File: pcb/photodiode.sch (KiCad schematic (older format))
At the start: 9 parts, among them U6 photodiode, U7 LM324N

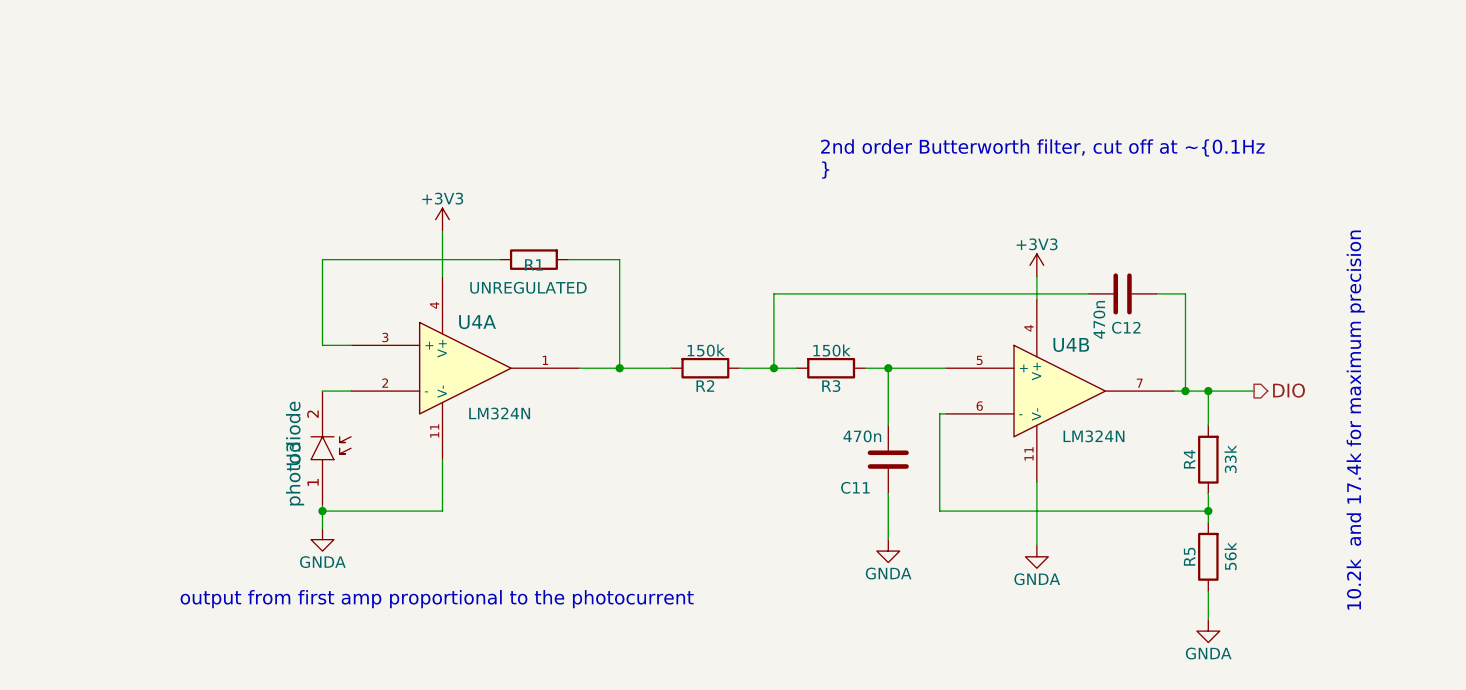
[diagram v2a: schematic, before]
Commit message: Changes to board, add footprints
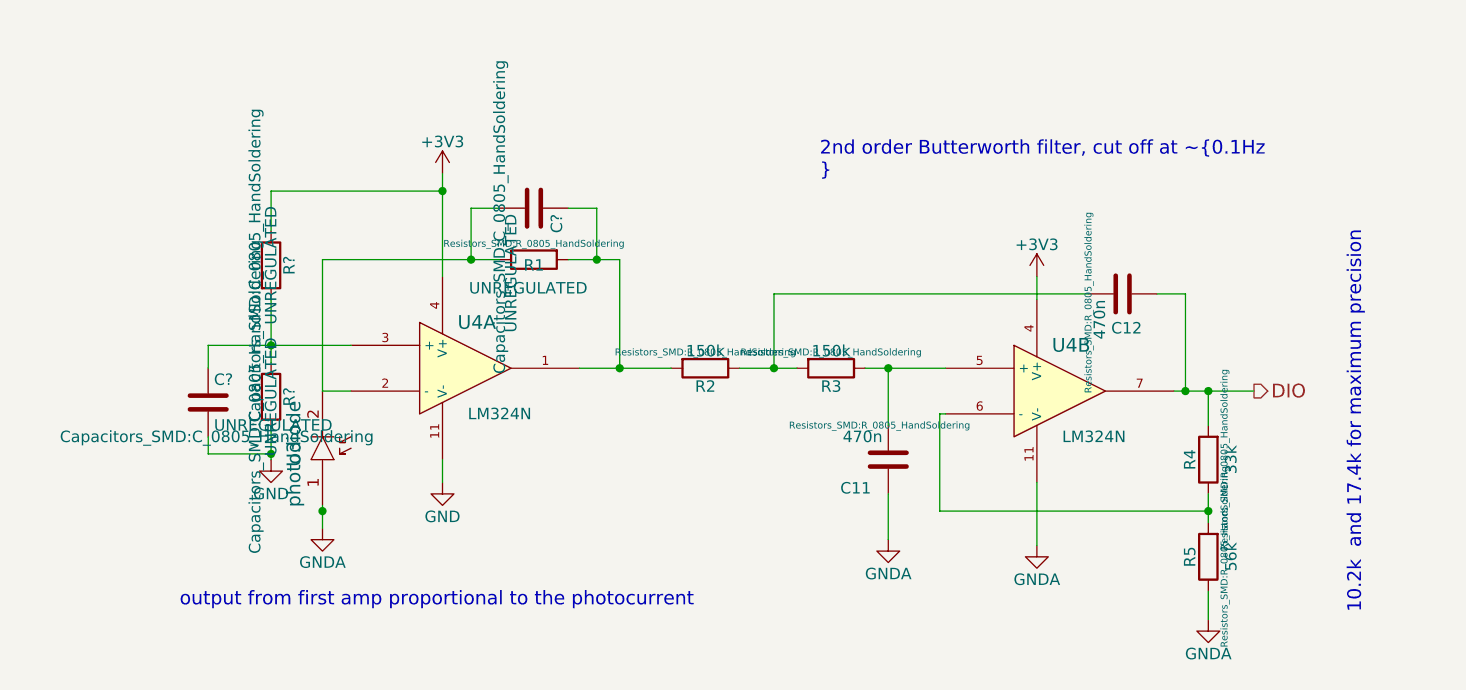
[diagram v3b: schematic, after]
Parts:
- added C? (x2): UNREGULATED, Capacitors_SMD:C_0805_HandSoldering, symbol C
- added R? (x2): UNREGULATED, Capacitors_SMD:C_0805_HandSoldering, symbol R
- C11, C16, R11, R12, R13, R14, R15: footprint (none) -> Resistors_SMD:R_0805_HandSoldering
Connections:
- net +3V3: now also R?.1
- net GNDA: no longer U7.11 (V-)
- net at U6.2 (C), U7.2 (-): now also R11.1, C?.2
- net at U7.3 (+): now also C?.1, R?.1, R?.2; no longer R11.1
- net at R11.2, R12.2, U7.1: now also C?.1
- new net GND: C?.2, R?.2, U7.11 (V-)
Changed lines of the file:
@@
 F 0 "R1" V 4425 2750 50  0000 C CNN
 F 1 "UNREGULATED" V 4525 2775 50  0000 C CNN
-F 2 "" V 4330 2750 30  0000 C CNN
+F 2 "Resistors_SMD:R_0805_HandSoldering" V 4330 2750 30  0000 C CNN
 F 3 "" H 4400 2750 30  0000 C CNN
 	1    4400 2750
@@
 L +3V3 #PWR40
 U 1 1 55BD9EDC
-P 4000 2625
+P 4000 2375
 AR Path="/55BDA44F/55BD9EDC" Ref="#PWR40"  Part="1"
 AR Path="/55BD9D56/55BD9EDC" Ref="#PWR28"  Part="1"
 AR Path="/55BDA313/55BD9EDC" Ref="#PWR34"  Part="1"
 AR Path="/55BDA511/55BD9EDC" Ref="#PWR46"  Part="1"
-F 0 "#PWR28" H 4000 2475 50  0001 C CNN
-F 1 "+3V3" H 4000 2765 50  0000 C CNN
-F 2 "" H 4000 2625 60  0000 C CNN
-F 3 "" H 4000 2625 60  0000 C CNN
-	1    4000 2625
+F 0 "#PWR28" H 4000 2225 50  0001 C CNN
+F 1 "+3V3" H 4000 2515 50  0000 C CNN
+F 2 "" H 4000 2375 60  0000 C CNN
+F 3 "" H 4000 2375 60  0000 C CNN
+	1    4000 2375
 	1    0    0    -1
 $EndComp
@@
 F 0 "R3" V 5780 3225 50  0000 C CNN
 F 1 "150k" V 5625 3225 50  0000 C CNN
-F 2 "" V 5630 3225 30  0000 C CNN
+F 2 "Resistors_SMD:R_0805_HandSoldering" V 5630 3225 30  0000 C CNN
 F 3 "" H 5700 3225 30  0000 C CNN
 	1    5700 3225
@@
 F 0 "R4" V 7430 3625 50  0000 C CNN
 F 1 "33k" V 7250 3625 50  0000 C CNN
-F 2 "" V 7280 3625 30  0000 C CNN
+F 2 "Resistors_SMD:R_0805_HandSoldering" V 7280 3625 30  0000 C CNN
 F 3 "" H 7350 3625 30  0000 C CNN
 F 4 "Farnell" V 7350 3625 60  0001 C CNN "Supplier"
@@
 F 0 "R2" V 5230 3225 50  0000 C CNN
 F 1 "150k" V 5075 3225 50  0000 C CNN
-F 2 "" V 5080 3225 30  0000 C CNN
+F 2 "Resistors_SMD:R_0805_HandSoldering" V 5080 3225 30  0000 C CNN
 F 3 "" H 5150 3225 30  0000 C CNN
 	1    5150 3225
@@
 F 0 "R5" V 7430 4050 50  0000 C CNN
 F 1 "56k" V 7250 4050 50  0000 C CNN
-F 2 "" V 7280 4050 30  0000 C CNN
+F 2 "Resistors_SMD:R_0805_HandSoldering" V 7280 4050 30  0000 C CNN
 F 3 "" H 7350 4050 30  0000 C CNN
 F 4 "Farnell" V 7350 4050 60  0001 C CNN "Supplier"
@@
 F 0 "C12" V 7125 2850 50  0000 L CNN
 F 1 "470n" H 7000 2800 50  0000 L CNN
-F 2 "" H 7013 2750 30  0000 C CNN
+F 2 "Resistors_SMD:R_0805_HandSoldering" H 7013 2750 30  0000 C CNN
 F 3 "" H 6975 2900 60  0000 C CNN
 F 4 "Farnell" V 6975 2900 60  0001 C CNN "Supplier"
@@
 $EndComp
 Wire Wire Line
-	3475 3825 3475 3925
+	3475 3825 3475 3850
+Wire Wire Line
+	3475 3850 3475 3925
 Wire Wire Line
 	3475 3325 3600 3325
 Wire Wire Line
-	4600 3225 5000 3225
+	4600 3225 4775 3225
+Wire Wire Line
+	4775 3225 5000 3225
 Wire Wire Line
 	4775 3225 4775 2750
 Wire Wire Line
-	4775 2750 4550 2750
+	4775 2750 4675 2750
+Wire Wire Line
+	4675 2750 4550 2750
 Connection ~ 4775 3225
-Wire Wire Line
-	4250 2750 3475 2750
-Wire Wire Line
-	3475 2750 3475 3125
-Wire Wire Line
-	3475 3125 3600 3125
-Wire Wire Line
-	4000 3625 4000 3850
-Wire Wire Line
-	4000 3850 3475 3850
 Connection ~ 3475 3850
 Wire Wire Line
-	4000 2825 4000 2625
-Wire Wire Line
-	5300 3225 5550 3225
-Wire Wire Line
-	5850 3225 6200 3225
+	4000 2375 4000 2450
+Wire Wire Line
+	4000 2450 4000 2825
+Wire Wire Line
+	5300 3225 5450 3225
+Wire Wire Line
+	5450 3225 5550 3225
+Wire Wire Line
+	5850 3225 5950 3225
+Wire Wire Line
+	5950 3225 6200 3225
 Wire Wire Line
 	5950 3475 5950 3225
@@
 	5950 3775 5950 3975
 Wire Wire Line
-	7200 3325 7550 3325
+	7200 3325 7250 3325
+Wire Wire Line
+	7250 3325 7350 3325
+Wire Wire Line
+	7350 3325 7550 3325
 Wire Wire Line
 	7350 3325 7350 3475
 Connection ~ 7350 3325
 Wire Wire Line
-	7350 3775 7350 3900
+	7350 3775 7350 3850
+Wire Wire Line
+	7350 3850 7350 3900
 Wire Wire Line
 	7350 4200 7350 4325
@@
 F 0 "C11" H 6025 3750 50  0000 L CNN
 F 1 "470n" H 5975 3525 50  0000 L CNN
-F 2 "" H 5988 3475 30  0000 C CNN
+F 2 "Resistors_SMD:R_0805_HandSoldering" H 5988 3475 30  0000 C CNN
 F 3 "" H 5950 3625 60  0000 C CNN
 F 4 "Farnell" V 5950 3625 60  0001 C CNN "Supplier"
@@
 Text Notes 8025 4300 1    60   ~ 0
 10.2k  and 17.4k for maximum precision
+$Comp
+L GND #PWR?
+U 1 1 58B5F33A
+P 4000 3725
+F 0 "#PWR?" H 4000 3475 50  0001 C CNN
+F 1 "GND" H 4000 3575 50  0000 C CNN
+F 2 "" H 4000 3725 50  0000 C CNN
+F 3 "" H 4000 3725 50  0000 C CNN
+	1    4000 3725
+	1    0    0    -1
+$EndComp
+Wire Wire Line
+	4000 3625 4000 3725
+Wire Wire Line
+	4250 2750 4125 2750
+Wire Wire Line
+	4125 2750 3475 2750
+Wire Wire Line
+	3475 2750 3475 3325
+Wire Wire Line
+	4000 2450 3250 2450
+Wire Wire Line
+	3250 2450 3250 2625
+Connection ~ 4000 2450
+$Comp
+L R R?
+U 1 1 58B5F491
+P 3250 2775
+F 0 "R?" V 3330 2775 50  0000 C CNN
+F 1 "UNREGULATED" V 3250 2775 50  0000 C CNN
+F 2 "Capacitors_SMD:C_0805_HandSoldering" V 3180 2775 50  0000 C CNN
+F 3 "" H 3250 2775 50  0000 C CNN
+	1    3250 2775
+	1    0    0    -1
+$EndComp
+$Comp
+L R R?
+U 1 1 58B5F4E6
+P 3250 3350
+F 0 "R?" V 3330 3350 50  0000 C CNN
+F 1 "UNREGULATED" V 3250 3350 50  0000 C CNN
+F 2 "Capacitors_SMD:C_0805_HandSoldering" V 3180 3350 50  0000 C CNN
+F 3 "" H 3250 3350 50  0000 C CNN
+	1    3250 3350
+	1    0    0    -1
+$EndComp
+$Comp
+L GND #PWR?
+U 1 1 58B5F64D
+P 3250 3625
+F 0 "#PWR?" H 3250 3375 50  0001 C CNN
+F 1 "GND" H 3250 3475 50  0000 C CNN
+F 2 "" H 3250 3625 50  0000 C CNN
+F 3 "" H 3250 3625 50  0000 C CNN
+	1    3250 3625
+	1    0    0    -1
+$EndComp
+Wire Wire Line
+	3250 2925 3250 3125
+Wire Wire Line
+	3250 3125 3250 3200
+Wire Wire Line
+	3250 3500 3250 3600
+Wire Wire Line
+	3250 3600 3250 3625
+Wire Wire Line
+	2975 3125 3250 3125
+Wire Wire Line
+	3250 3125 3600 3125
+Connection ~ 3250 3125
+$Comp
+L C C?
+U 1 1 58B5F740
+P 4400 2525
+F 0 "C?" H 4425 2625 50  0000 L CNN
+F 1 "UNREGULATED" H 4425 2425 50  0000 L CNN
+F 2 "Capacitors_SMD:C_0805_HandSoldering" H 4438 2375 50  0000 C CNN
+F 3 "" H 4400 2525 50  0000 C CNN
+	1    4400 2525
+	0    1    1    0
+$EndComp
+Wire Wire Line
+	4125 2750 4125 2525
+Wire Wire Line
+	4125 2525 4250 2525
+Connection ~ 4125 2750
+Wire Wire Line
+	4550 2525 4675 2525
+Wire Wire Line
+	4675 2525 4675 2750
+Connection ~ 4675 2750
+$Comp
+L C C?
+U 1 1 58B5F815
+P 2975 3375
+F 0 "C?" H 3000 3475 50  0000 L CNN
+F 1 "UNREGULATED" H 3000 3275 50  0000 L CNN
+F 2 "Capacitors_SMD:C_0805_HandSoldering" H 3013 3225 50  0000 C CNN
+F 3 "" H 2975 3375 50  0000 C CNN
+	1    2975 3375
+	1    0    0    -1
+$EndComp
+Wire Wire Line
+	2975 3225 2975 3125
+Wire Wire Line
+	2975 3525 2975 3600
+Wire Wire Line
+	2975 3600 3250 3600
+Connection ~ 3250 3600
 $EndSCHEMATC
